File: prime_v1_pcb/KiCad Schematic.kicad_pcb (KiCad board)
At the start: 4 copper layers, 70 x 100 mm, 195 parts, among them IC1 AP63205WU-7, IC2 ATSAMD51J19A-MU, IC4 TMC5160A-TA-T, IC6 TMC5160A-TA-T, IC7 TMC5160A-TA-T, J1 Conn_01x04, J13 Conn_01x10, J14 Conn_01x04, J15 Conn_01x03, J16 Conn_01x03, J17 Hole, J18 Hole, J19 Hole, J2 691313710002, J20 Hole, J22 Conn_01x06, J23 Conn_01x04, J24 Conn_01x04, J25 Conn_01x05, J26 Conn_01x05, J27 Conn_01x05, J3 47346-0001, J4 Conn_01x04, J5 Conn_01x04, J6 20021121-00010C4LF, J7 Conn_01x04, J8 Conn_01x05, J9 Conn_01x04, Q13 FDMC8030, Q14 FDMC8030, Q15 FDMC8030, Q16 FDMC8030, Q17 FDMC8030, Q18 FDMC8030, Q19 FDMC8030, Q20 FDMC8030, Q5 FDMC8030, Q6 FDMC8030, Q7 FDMC8030, Q8 FDMC8030, U1 TMC2041-LA, U2 TMC2041-LA, U3 AP2112K-3.3, Y1 LFXTAL009678REEL

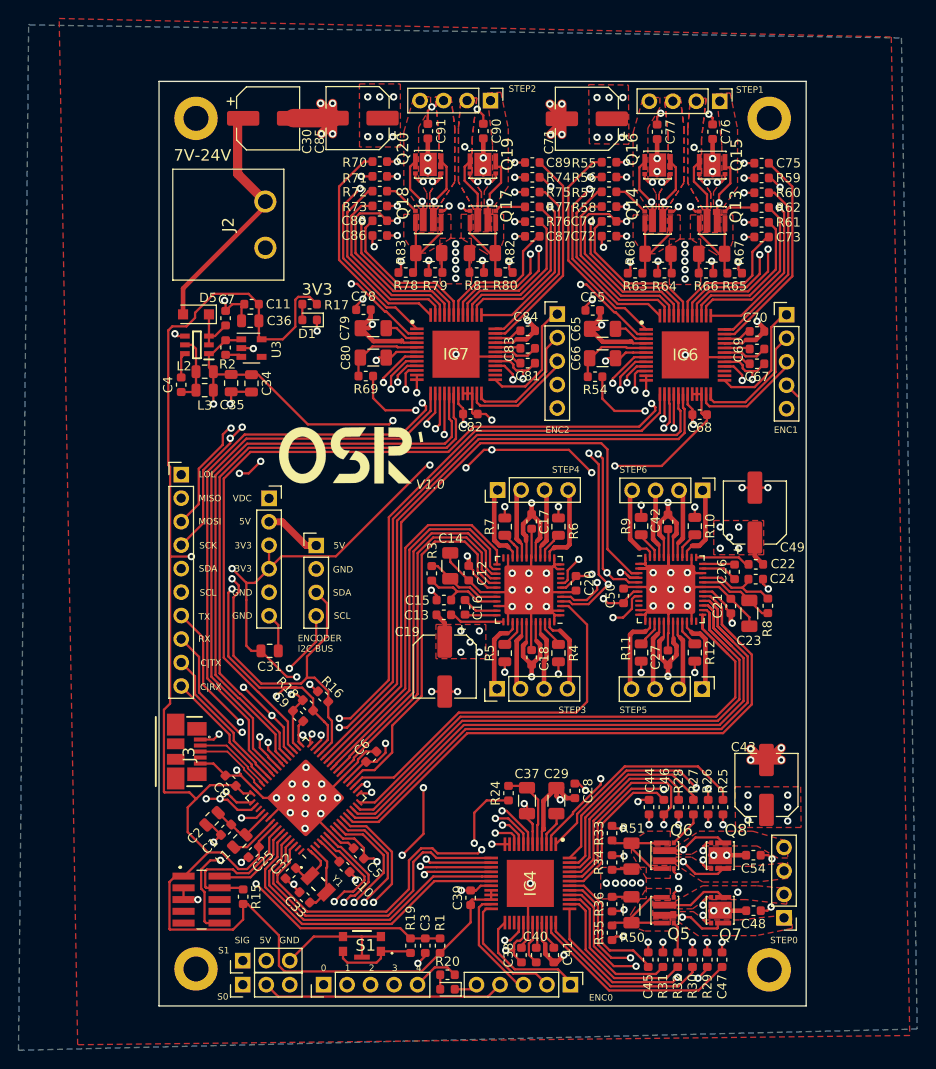
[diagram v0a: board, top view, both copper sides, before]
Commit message: some work fixing board, bump arduino package version
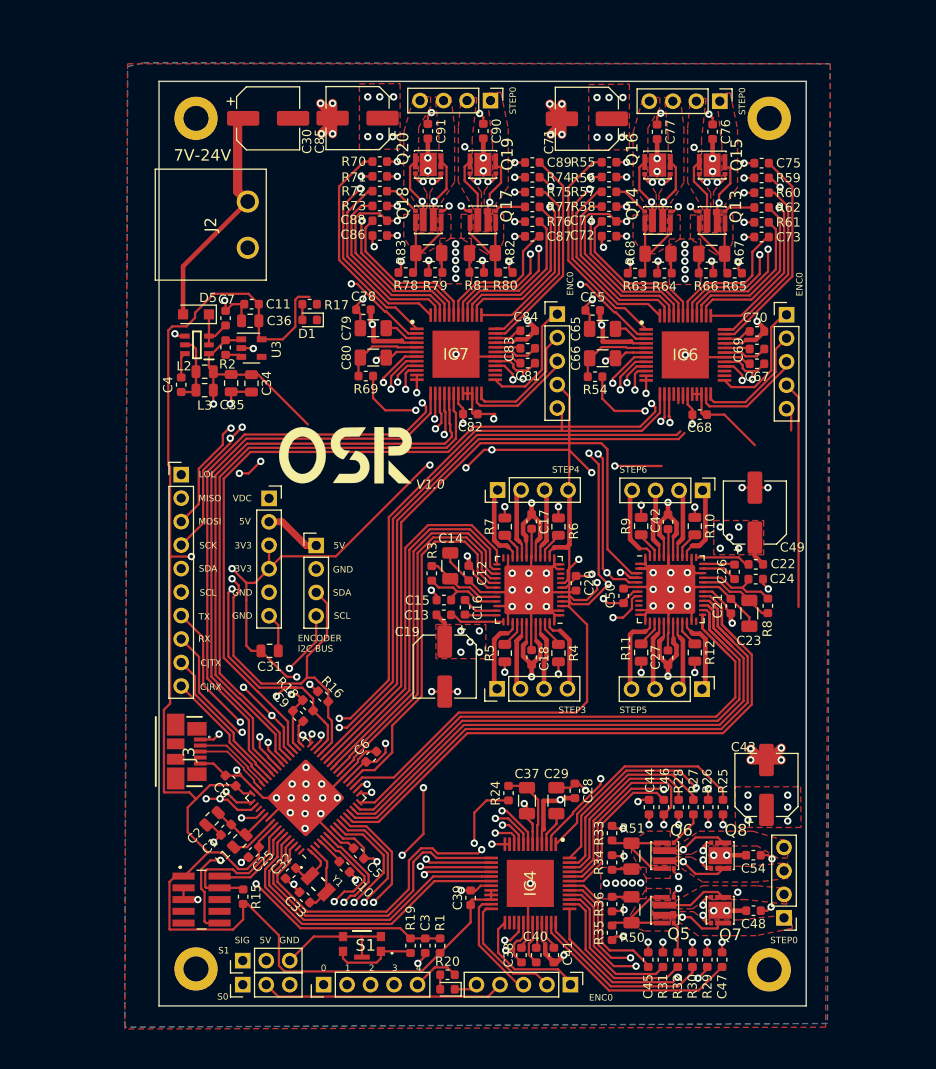
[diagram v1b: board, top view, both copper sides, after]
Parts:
- moved J2 1.90 mm to (55.5, 121.0)
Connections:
- C29 pad 1: +VDC -> GND
- C65 pad 1: +VDC -> GND
- C79 pad 1: +VDC -> GND
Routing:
- net +VDC: track 356.0 -> 563.7 mm
- net /SCK: track 167.0 -> 156.2 mm
- net +5V: track 188.8 -> 179.6 mm, vias 3 -> 2
- net /MISO: track 176.1 -> 171.7 mm, vias 8 -> 7
- net /D1_DIR: track 69.2 -> 64.9 mm
- net /D1_STEP: track 69.6 -> 65.5 mm
- net GND: track 294.1 -> 296.4 mm, vias 106 -> 105
- net /sheet61C22781/S0_2A: track 41.7 -> 39.9 mm
- net /sheet61BB23C4/S0_2A: track 41.7 -> 39.9 mm
- net +3V3: track 329.1 -> 327.9 mm
- net /D2_DIR: track 66.7 -> 65.7 mm
- net /D2_STEP: track 67.1 -> 66.1 mm
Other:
- board text removed: "'"
- board text removed: "ENC1"
- board text removed: "ENC2"
- board text removed: "STEP1"
- board text removed: "STEP2"
